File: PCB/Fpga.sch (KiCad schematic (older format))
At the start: 7 parts, among them U4 10CL016YE144C8G

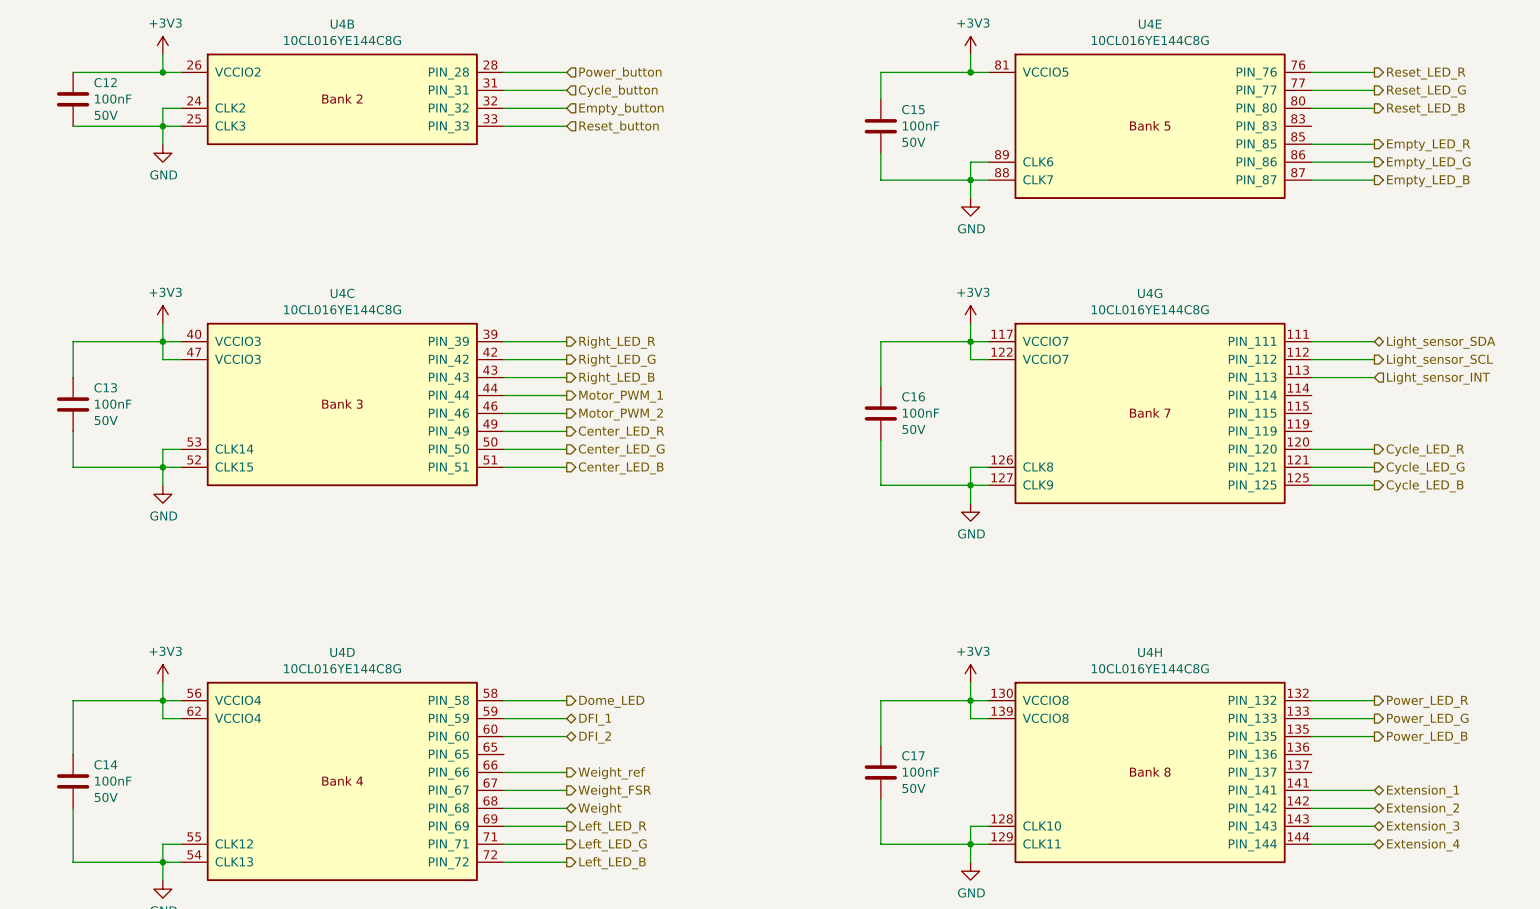
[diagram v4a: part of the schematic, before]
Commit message: Add support for the hall sensors and dome LED
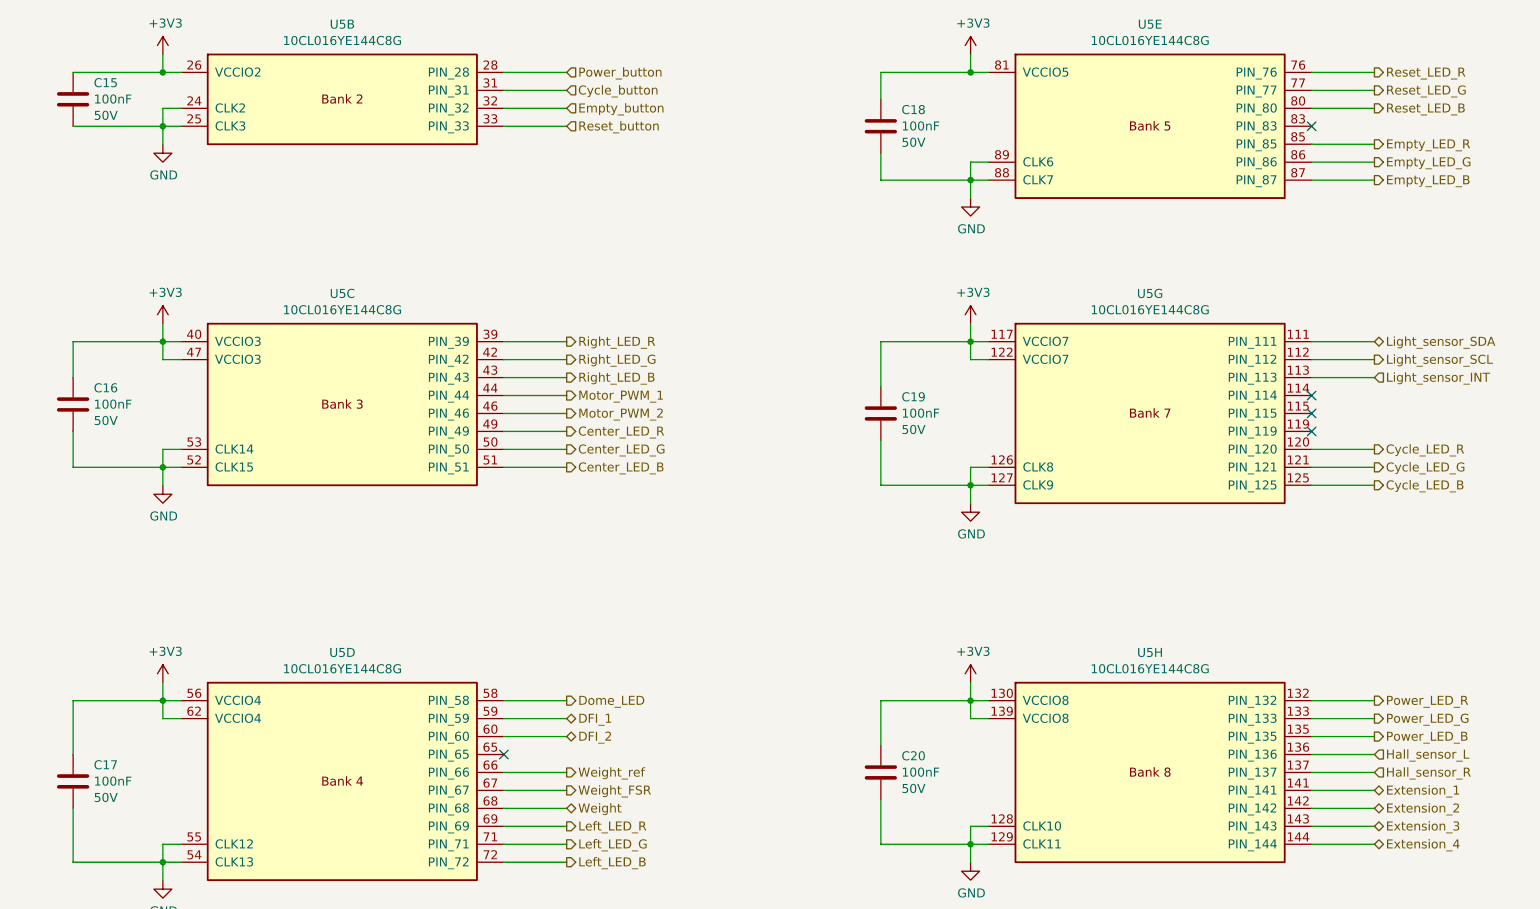
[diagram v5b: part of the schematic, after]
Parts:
- renumbered C12 to C15, C13 to C16, C14 to C17, C15 to C18, C16 to C19, C17 to C20, U4 to U5
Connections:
- net Hall_sensor_L: now reaches U5.136 (PIN_136)
- net Hall_sensor_R: now reaches U5.137 (PIN_137)
- no-connect marks 0 -> 5

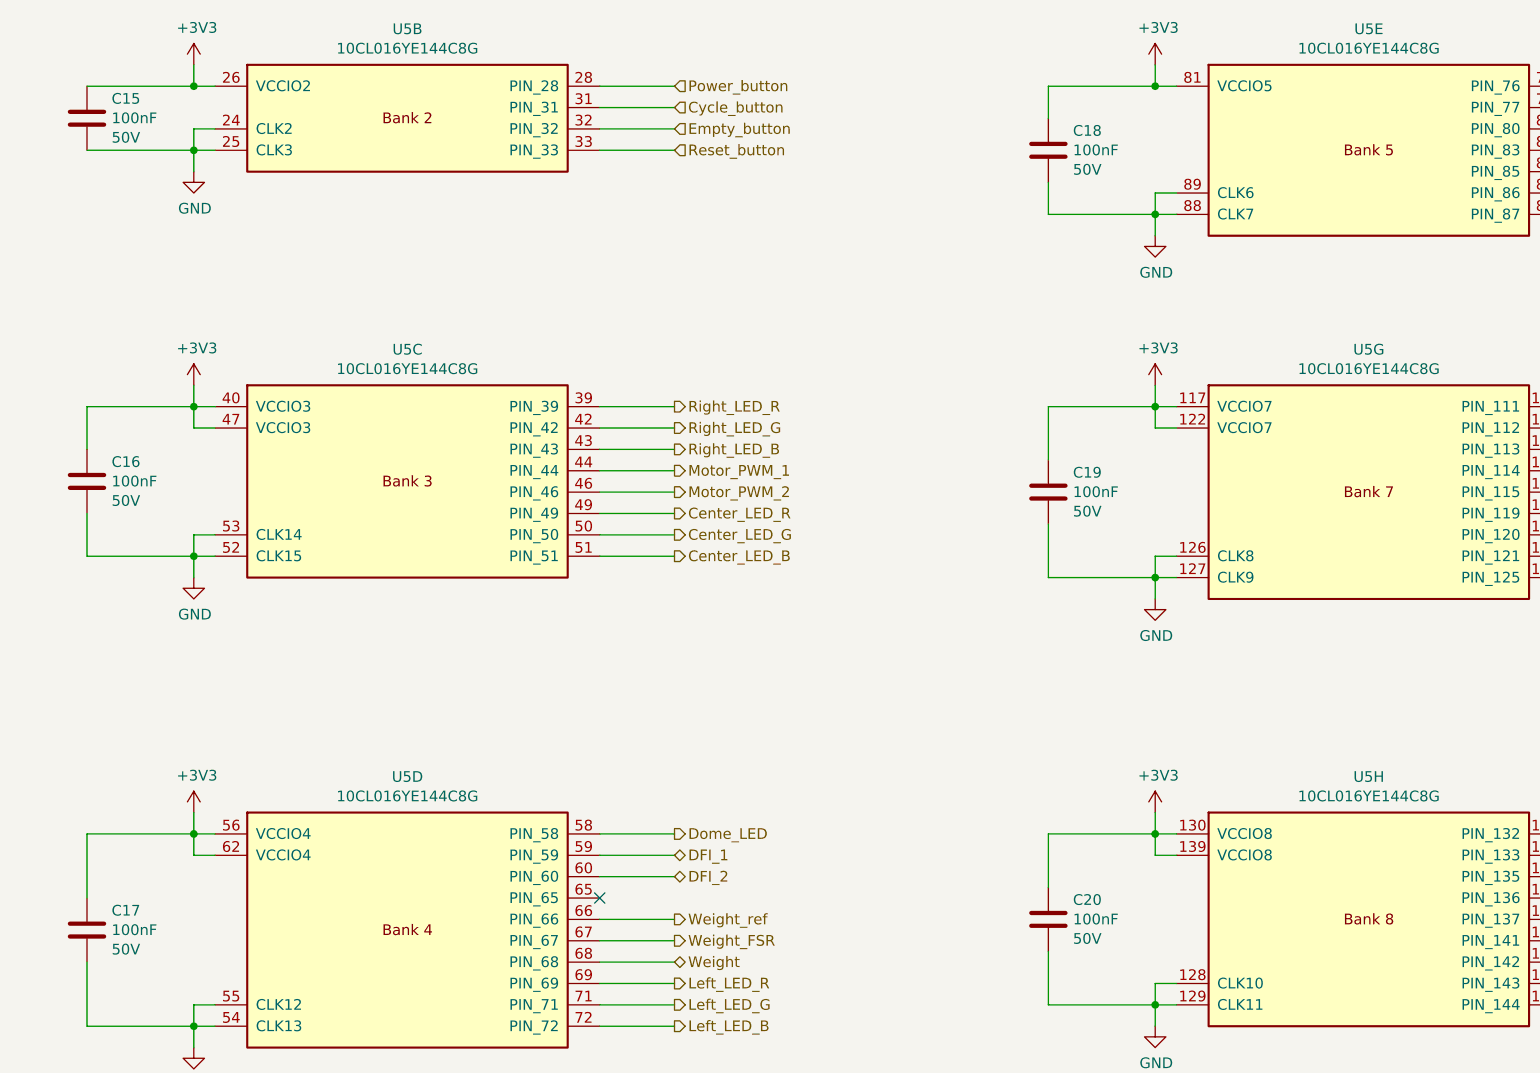
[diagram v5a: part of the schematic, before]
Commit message: Re-annotate all components
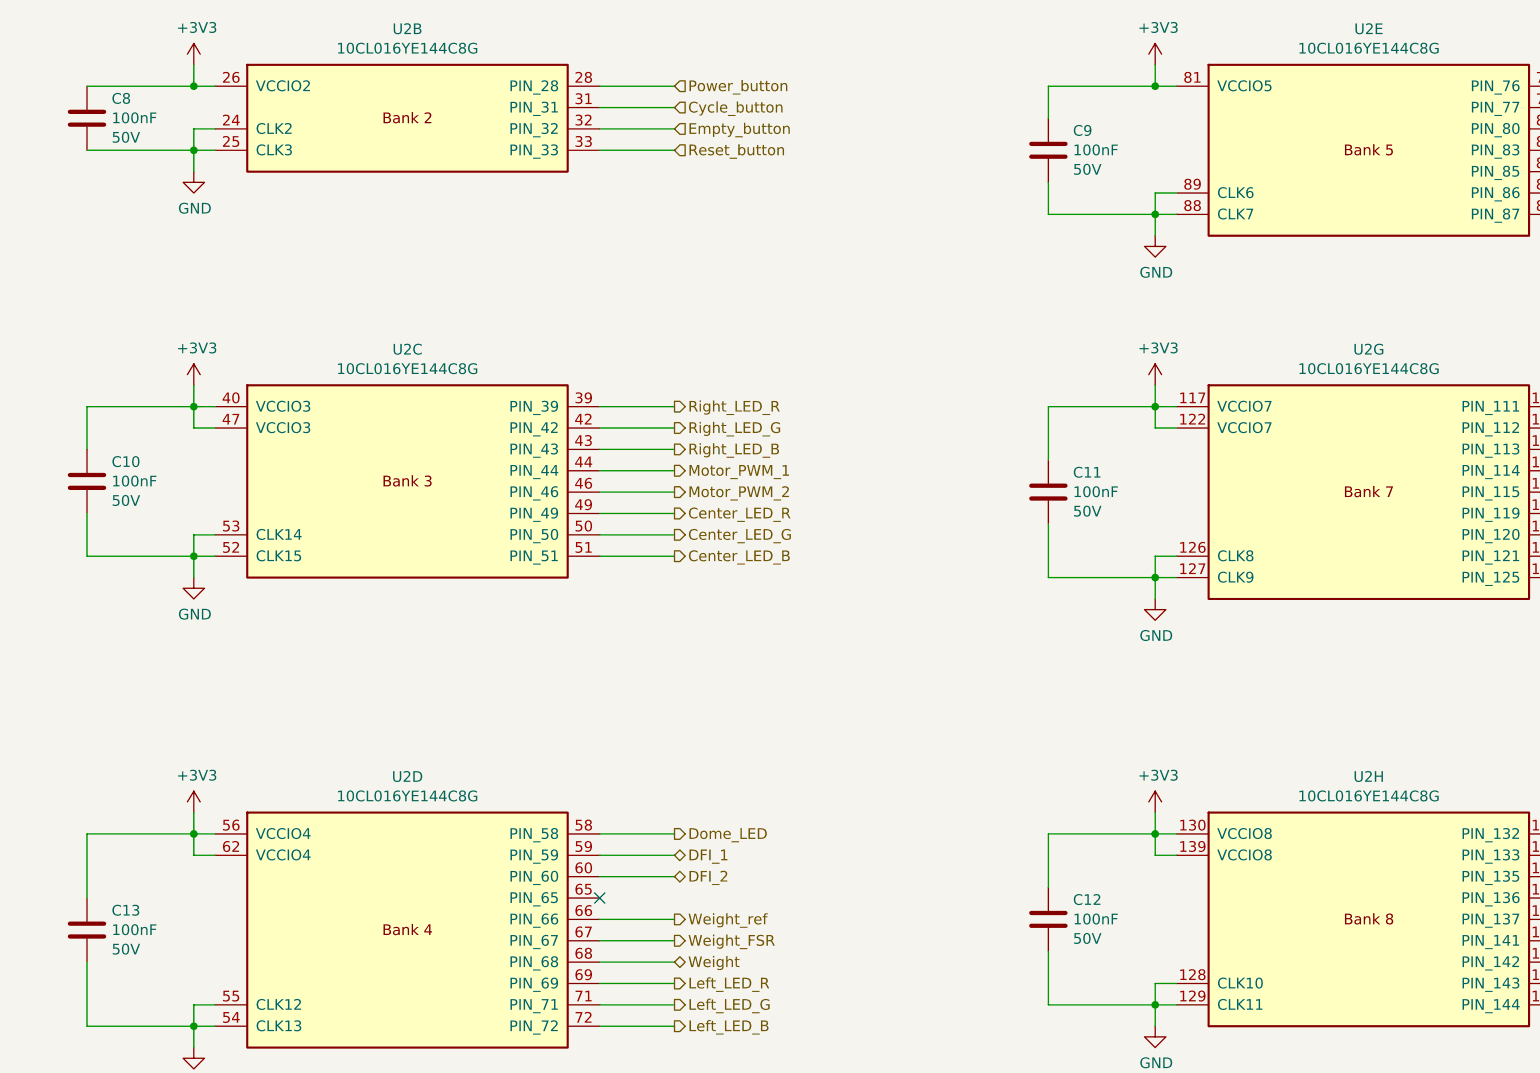
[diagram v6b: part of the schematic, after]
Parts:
- renumbered C16 to C10, C19 to C11, C20 to C12, C17 to C13, C15 to C8, C18 to C9, U5 to U2

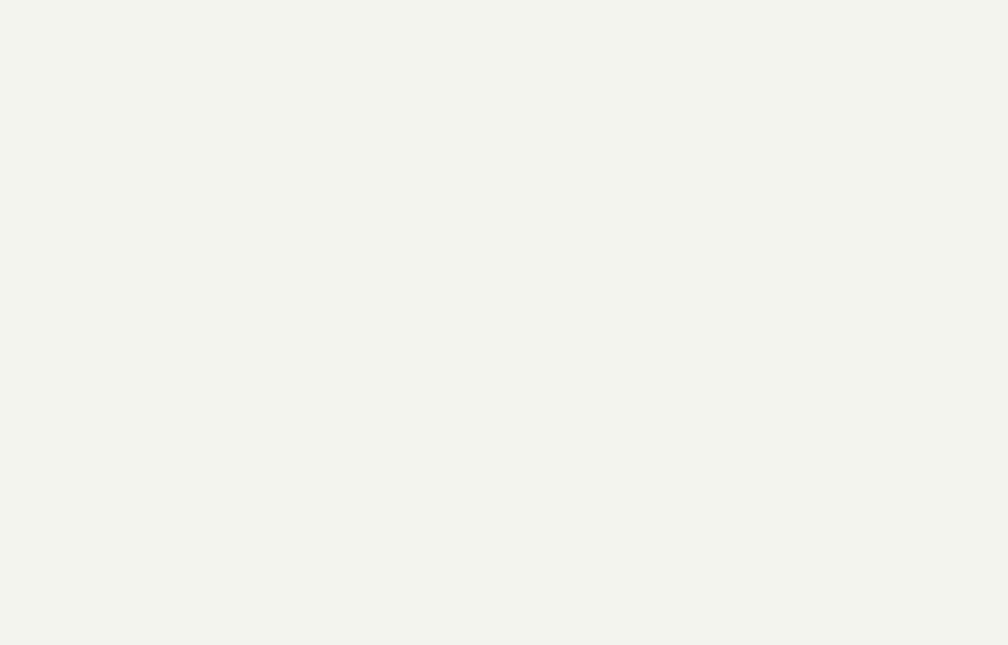
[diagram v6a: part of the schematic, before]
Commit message: Add the EMB1061 Bluetooth module
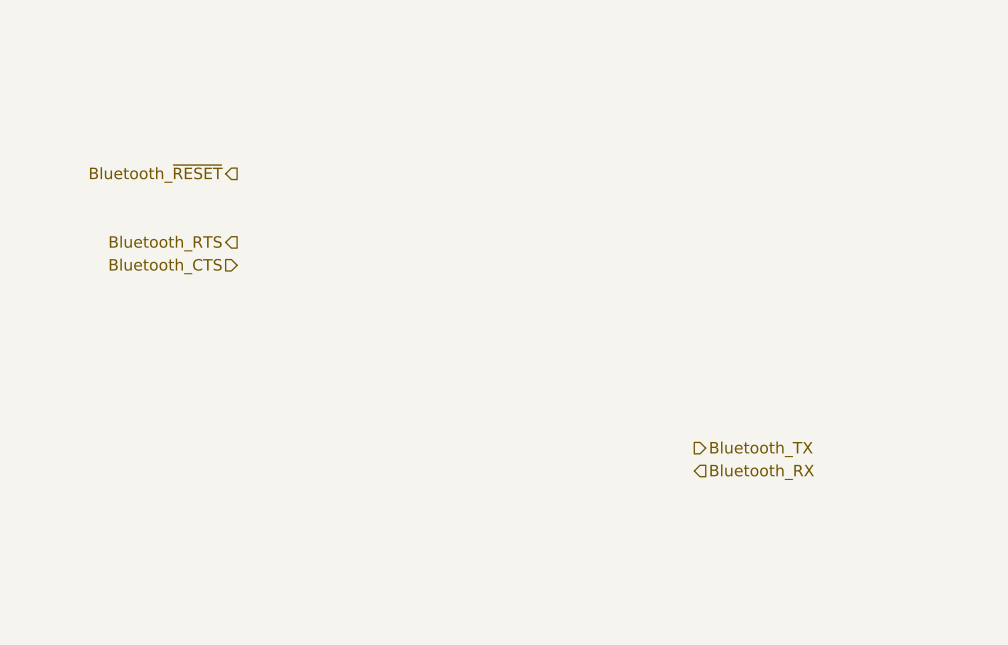
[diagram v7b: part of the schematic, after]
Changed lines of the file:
@@
 $Descr A4 11693 8268
 encoding utf-8
-Sheet 3 22
+Sheet 3 23
 Title "Litter Robot 3 - FPGA"
-Date "2021-04-05"
+Date "2021-04-10"
 Rev "A1"
 Comp "L. Sartory"
@@
 NoConn ~ 8650 1400
 NoConn ~ 4150 4900
+Text HLabel -1050 5100 2    50   Output ~ 0
+Bluetooth_TX
+Text HLabel -1050 5200 2    50   Input ~ 0
+Bluetooth_RX
+Text HLabel -3050 4300 0    50   Input ~ 0
+Bluetooth_CTS
+Text HLabel -3050 4200 0    50   Output ~ 0
+Bluetooth_RTS
+Text HLabel -3050 3900 0    50   Output ~ 0
+Bluetooth_~RESET
 $EndSCHEMATC

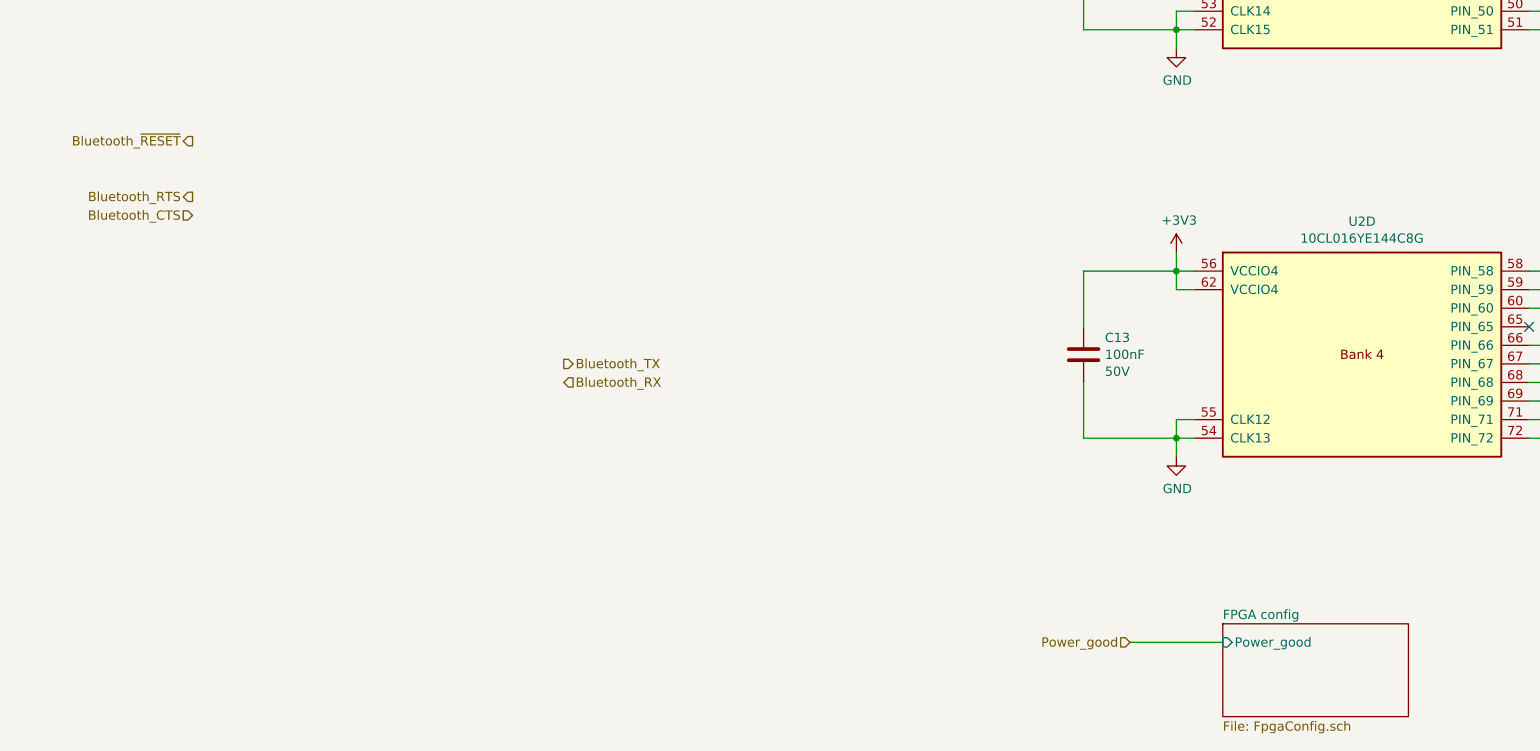
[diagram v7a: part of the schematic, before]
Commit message: Connect the Bluetooth module to the FPGA
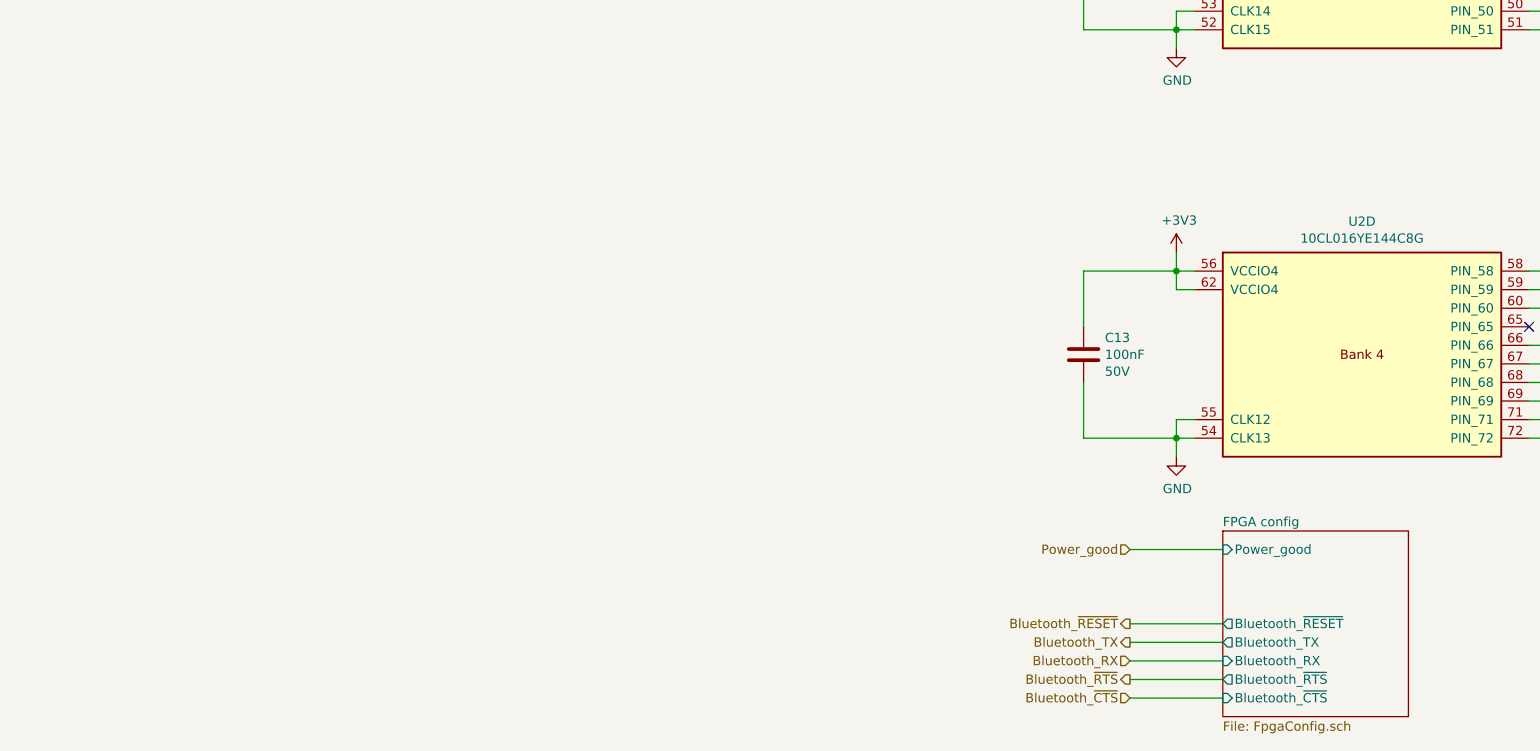
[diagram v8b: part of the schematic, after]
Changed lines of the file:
@@
 Text HLabel 4500 1100 2    50   Input ~ 0
 Power_button
-Text HLabel 2000 6600 0    50   Input ~ 0
+Text HLabel 2000 6100 0    50   Input ~ 0
 Power_good
-Wire Wire Line
-	2000 6600 2500 6600
 Text HLabel 9000 4800 2    50   Output ~ 0
 Power_LED_B
@@
 Light_sensor_INT
 $Sheet
-S 2500 6500 1000 500
+S 2500 6000 1000 1000
 U 60647CC2
 F0 "FPGA config" 50
 F1 "FpgaConfig.sch" 50
-F2 "Power_good" I L 2500 6600 50
+F2 "Power_good" I L 2500 6100 50
+F3 "Bluetooth_TX" O L 2500 6600 50
+F4 "Bluetooth_RX" I L 2500 6700 50
+F5 "Bluetooth_~CTS" I L 2500 6900 50
+F6 "Bluetooth_~RTS" O L 2500 6800 50
+F7 "Bluetooth_~RESET" O L 2500 6500 50
 $EndSheet
 $Sheet
@@
 NoConn ~ 8650 1400
 NoConn ~ 4150 4900
-Text HLabel -1050 5100 2    50   Output ~ 0
+Text HLabel 2000 6600 0    50   Output ~ 0
 Bluetooth_TX
-Text HLabel -1050 5200 2    50   Input ~ 0
+Text HLabel 2000 6700 0    50   Input ~ 0
 Bluetooth_RX
-Text HLabel -3050 4300 0    50   Input ~ 0
-Bluetooth_CTS
-Text HLabel -3050 4200 0    50   Output ~ 0
-Bluetooth_RTS
-Text HLabel -3050 3900 0    50   Output ~ 0
+Text HLabel 2000 6900 0    50   Input ~ 0
+Bluetooth_~CTS
+Text HLabel 2000 6800 0    50   Output ~ 0
+Bluetooth_~RTS
+Text HLabel 2000 6500 0    50   Output ~ 0
 Bluetooth_~RESET
+Wire Wire Line
+	2000 6600 2500 6600
+Wire Wire Line
+	2000 6800 2500 6800
+Wire Wire Line
+	2000 6700 2500 6700
+Wire Wire Line
+	2000 6500 2500 6500
+Wire Wire Line
+	2000 6100 2500 6100
+Wire Wire Line
+	2000 6900 2500 6900
 $EndSCHEMATC
